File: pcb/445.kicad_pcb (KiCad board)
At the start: 2 copper layers, 100 x 72 mm, 65 parts, among them J1 Screw_Terminal_01x01, J2 Screw_Terminal_01x01, J4 POT, J5 AVR-ISP-6, Q1 Q_NPN_BCE, Q2 BT136-500, SW1 Override switch, T1 Transformer_SP_1S, U1 UCC28720D, U2 TPS71533DCKR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

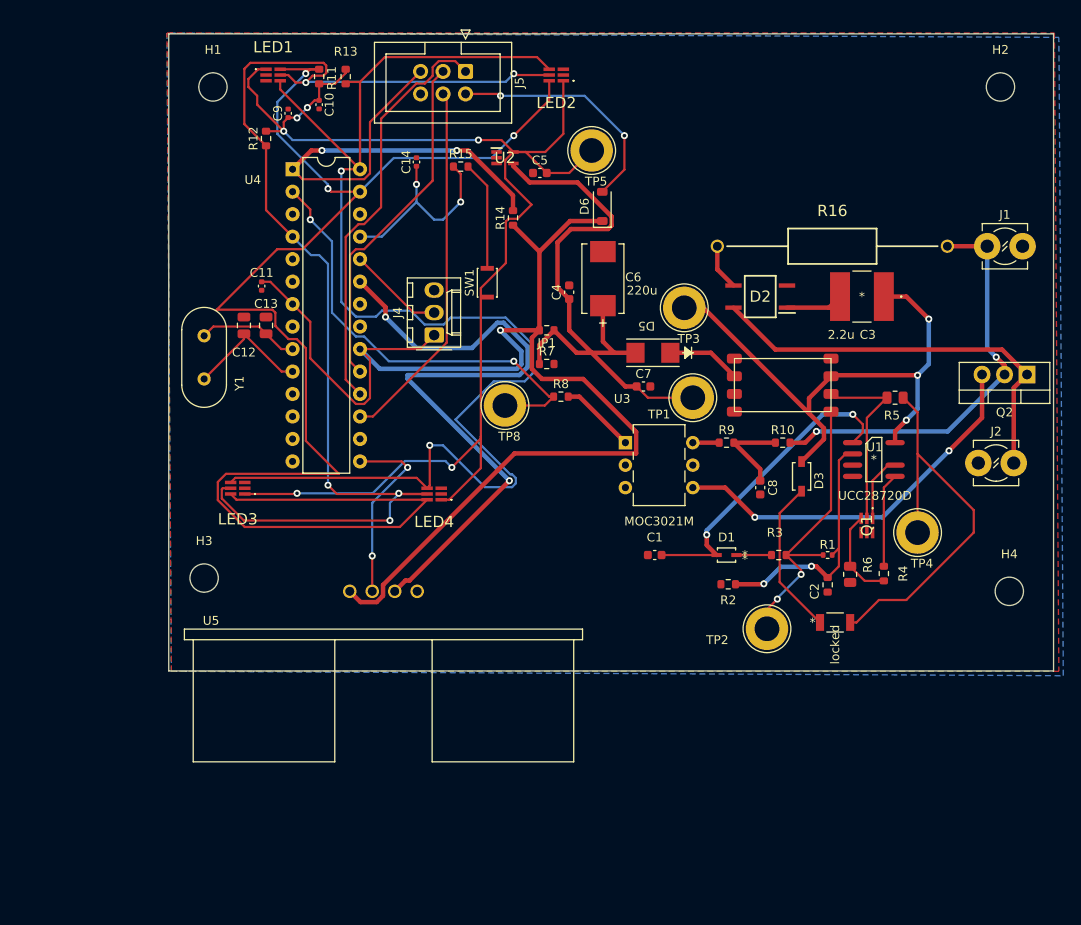
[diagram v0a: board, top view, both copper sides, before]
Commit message: Restructure project repository
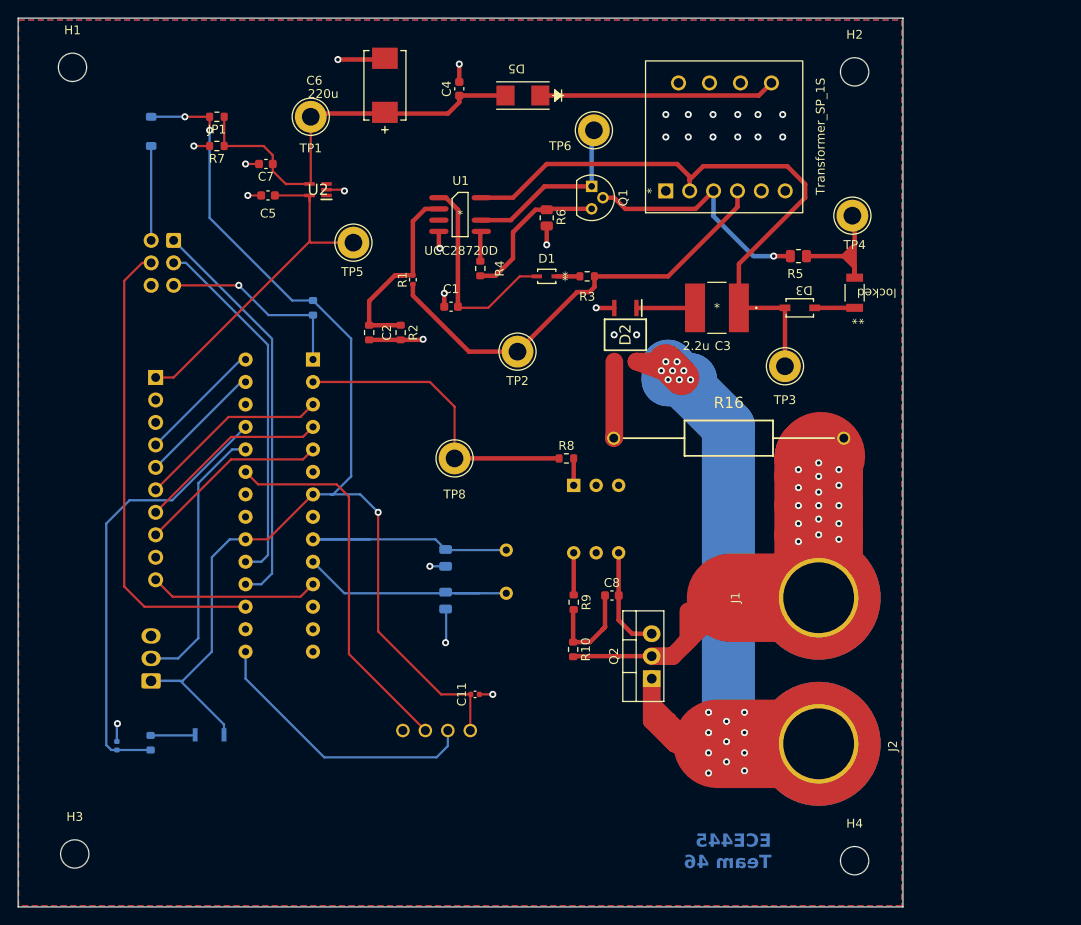
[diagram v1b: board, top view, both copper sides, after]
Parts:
- removed C10, C9: 1uF, Capacitor_SMD:C_0402_1005Metric
- removed LED1, LED2, LED3, LED4: ALS-DPDIC17-78C_L749_TR8, footprints:ALSDPDIC1778CL749TR8
- removed R11, R13: 1k, Resistor_SMD:R_0603_1608Metric
- removed R12: 10k, Resistor_SMD:R_0603_1608Metric
- added J3: Conn_01x10_Socket, Connector_PinSocket_2.54mm:PinSocket_1x10_P2.54mm_Vertical, B.Cu at (128.5, 68.8)
- added TP6: TestPoint, TestPoint:TestPoint_Loop_D3.80mm_Drill2.0mm, F.Cu at (178.1, 40.9)
- C12, C13, C14, D6, J4, J5, R14, R15, SW1, U3, U4, U5, Y1: moved to B.Cu
- J1, J2: footprint TerminalBlock_MetzConnect:TerminalBlock_MetzConnect_360410_1x01_Horizontal_ScrewM3.0 -> 445:MountingHole_8.0mm_M8_Pad_TopBottom
- Q1: footprint footprints:ALSDPDIC1778CL749TR8 -> Package_TO_SOT_THT:TO-92L
- R10: value 100 -> 470
- R8: value R -> 330
- R9: value 100 -> 360
- T1: footprint footprints:750317828 -> 445:750813314update
- TP1, TP2, TP3, TP4, TP5, TP8: footprint TestPoint:TestPoint_Loop_D3.80mm_Drill2.8mm -> TestPoint:TestPoint_Loop_D3.80mm_Drill2.0mm
- moved C14 74.2 mm to (124.1, 110.5)
- moved R15 73.9 mm to (128.0, 110.1), turned to 90 degrees
- moved SW1 60.0 mm to (134.6, 109.2), turned to 180 degrees
- moved C2 59.1 mm to (152.7, 63.8)
- moved R4 57.2 mm to (165.2, 56.5)
- moved R1 56.3 mm to (157.6, 57.8), turned to 90 degrees
- moved Q2 54.6 mm to (184.6, 102.9), turned to 90 degrees
- moved U1 54.3 mm to (162.9, 50.4)
- moved TP1 53.6 mm to (146.1, 39.4)
- moved R6 52.9 mm to (172.7, 50.8)
- moved C11 52.1 mm to (164.6, 104.6), turned to 180 degrees
- moved D6 51.7 mm to (128.0, 41.0), turned to -90 degrees
- moved J4 50.5 mm to (128.0, 103.1)
- moved C7 49.5 mm to (141.0, 44.7), turned to 180 degrees
- moved Q1 49.4 mm to (177.8, 47.2)
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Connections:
- C8 pad 2: GND -> Net-(Q2-G)
- SW1 pad 1: 3.3V linear regulator output -> Flyback output
- U4 pad 11: unconnected-(U4-PD5-Pad11) -> /Sensors/PD5
- U4 pad 3: unconnected-(U4-PD1-Pad3) -> /Sensors/PD1
- U4 pad 4: /Sensors/INT -> /Sensors/PD2
- U4 pad 5: unconnected-(U4-PD3-Pad5) -> /Sensors/PD3
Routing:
- net /Sensors/SDA: track 169.4 -> 14.2 mm, vias 3 -> 0
- net /Sensors/SCL: track 163.3 -> 14.0 mm, vias 2 -> 0
- net /Sensors/INT: track 136.4 -> 0.00 mm, vias 5 -> 0
- net 3.3V linear regulator output: track 150.6 -> 38.9 mm, vias 6 -> 0
- net Vac(-): track 46.9 -> 101.8 mm, vias 0 -> 19
- net /Sensors/Echo: track 76.1 -> 42.9 mm, vias 2 -> 0
- net Net-(Q2-G): track 43.6 -> 12.0 mm, vias 2 -> 0
- net /Sensors/RESET: track 53.0 -> 22.2 mm, vias 2 -> 1
- net /Sensors/Override signal: track 23.2 -> 50.5 mm, vias 2 -> 0
- net Net-(D4-Pad2): track 45.6 -> 18.8 mm
- net Net-(JP1-A): track 69.9 -> 47.0 mm
- net GND: track 0.00 -> 22.4 mm, vias 0 -> 10
- net /Sensors/PD3: track 0.00 -> 21.8 mm
- net /Sensors/PD2: track 0.00 -> 21.8 mm
- net /Sensors/PD1: track 0.00 -> 21.8 mm
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- added copper zone on B.Cu, net GND
- added copper zone on F.Cu, net GNDPWR
- removed copper zone on F.Cu, net GND
- removed copper zone on B.Cu, net GNDPWR
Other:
- board size 100 x 72 mm -> 100 x 100.4 mm
- board text added: "ECE445 Team 46"
